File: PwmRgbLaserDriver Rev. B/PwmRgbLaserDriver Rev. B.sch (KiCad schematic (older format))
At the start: 40 parts

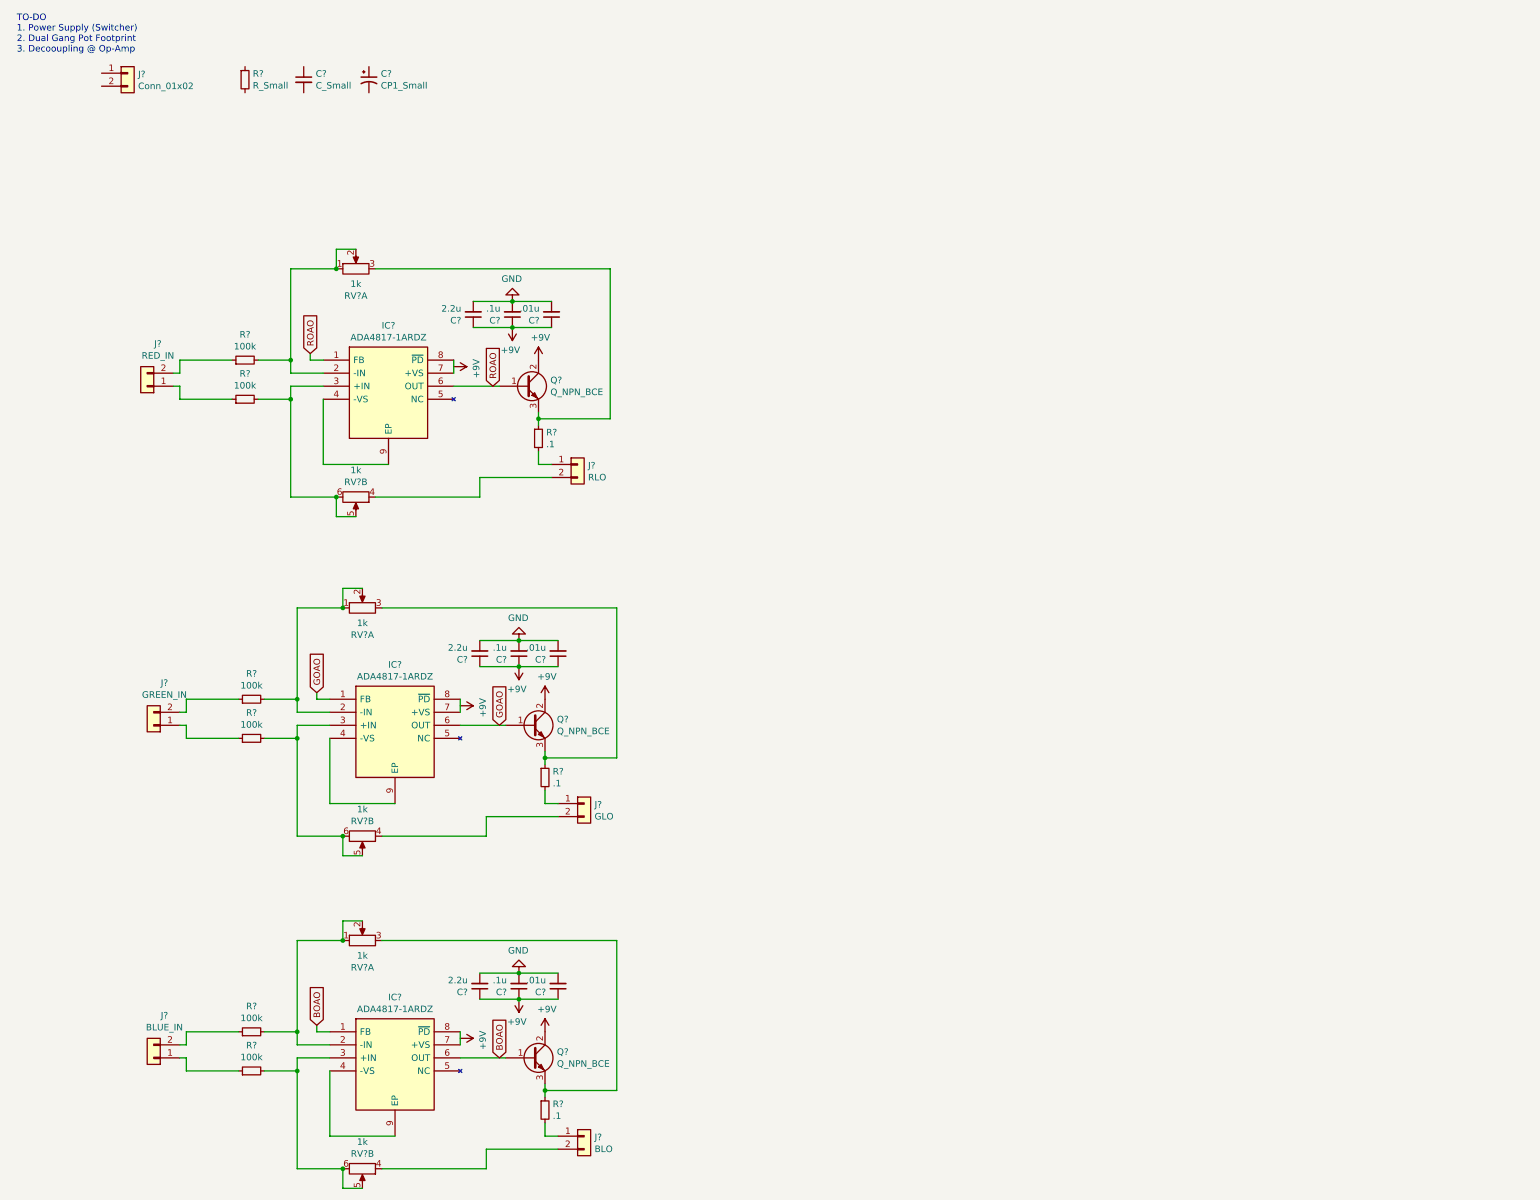
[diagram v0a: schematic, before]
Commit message: Switching Converter Added
This commit adds the switching converter for power.
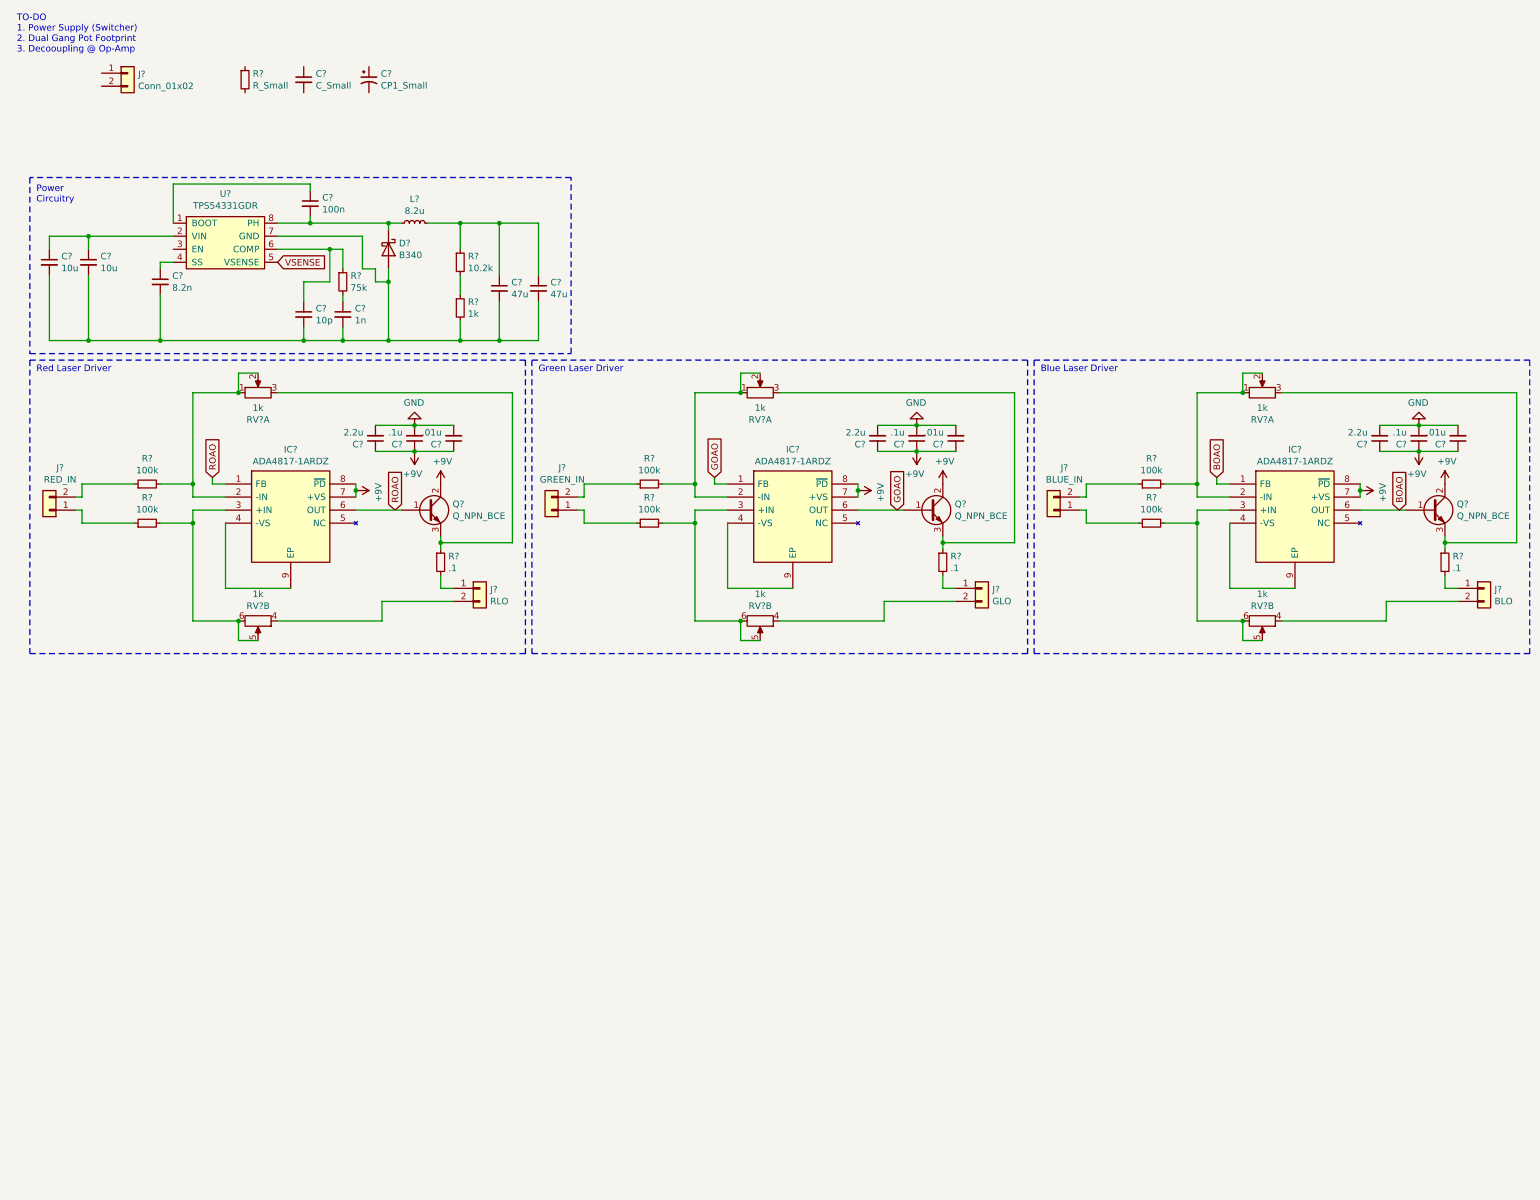
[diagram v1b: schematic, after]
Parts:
- added C?: 10p, symbol Device:C_Small
- added C?: 1n, symbol Device:C_Small
- added C?: 8.2n, symbol Device:C_Small
- added C? (x2): 47u, symbol Device:C_Small
- added C?: 100n, symbol Device:C_Small
- added C? (x2): 10u, symbol Device:C_Small
- added D?: B340, Diode_SMD:D_SMC, symbol Diode:B340
- added L?: 8.2u, symbol Device:L_Small
- added R?: 10.2k, symbol Device:R_Small
- added R?: 1k, symbol Device:R_Small
- added R?: 75k, symbol Device:R_Small
- added U?: TPS54331GDR, symbol SamacSys_Parts:TPS54331GDR
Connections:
- net +9V: now also IC?.7 (+VS), IC?.7 (+VS), IC?.7 (+VS), IC?.8 (~PD), IC?.8 (~PD), IC?.8 (~PD)
- new net: C?.1, U?.1 (BOOT)
- new net: C?.1, C?.1, U?.2 (VIN)
- new net: C?.1, U?.4 (SS)
- new net: C?.1, R?.1, U?.6 (COMP)
- new net: C?.2, C?.2, C?.2, C?.2, C?.2, C?.2, C?.2, D?.2 (A), R?.2, U?.7 (GND)
- new net: C?.2, D?.1 (K), L?.1, U?.8 (PH)
- new net: C?.1, R?.2
- new net: C?.1, C?.1, L?.2, R?.1
- new net: R?.1, R?.2
- new net VSENSE: U?.5 (VSENSE)
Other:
- note added: "Blue Laser Driver"
- note added: "Green Laser Driver"
- note added: "Power\nCircuitry"
- note added: "Red Laser Driver"
- moved on the sheet: C?, IC?, J?, Q?, R?, RV?A, RV?B

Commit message: Small Fixes
Added Enable pin resistor divider on switcher. Fixed grounding issues in drivers
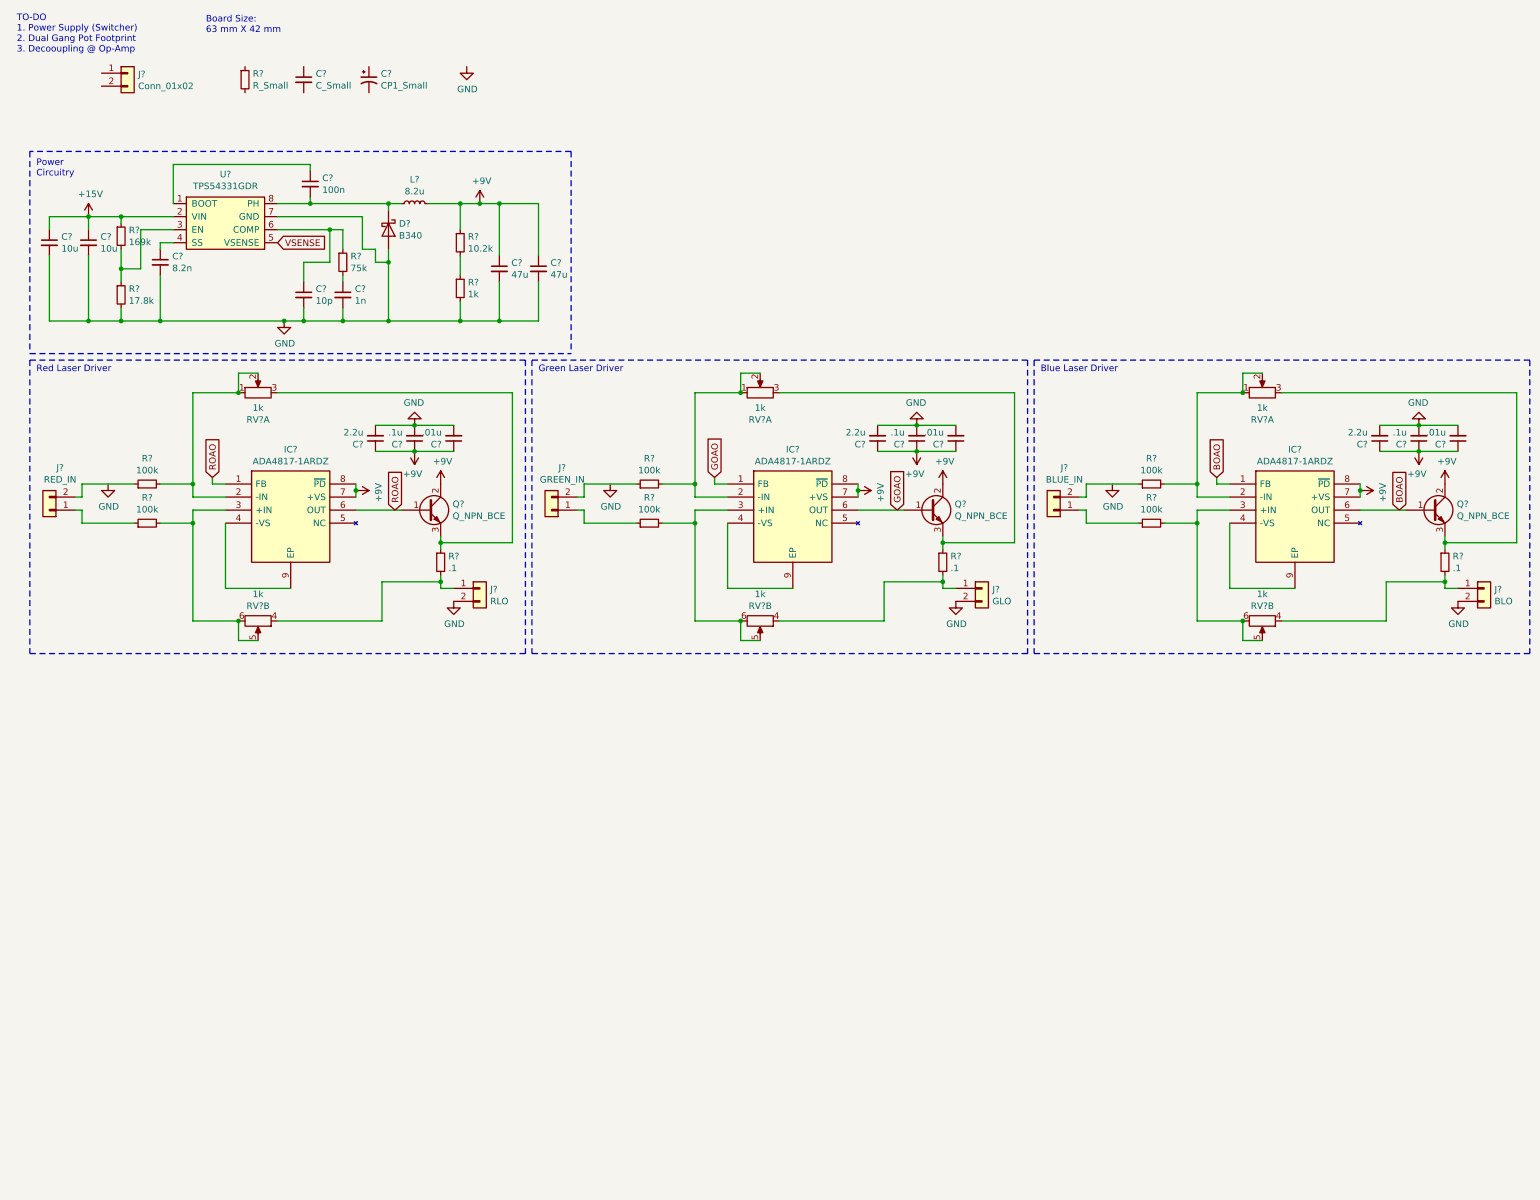
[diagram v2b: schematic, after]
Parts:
- added R?: 169k, symbol Device:R_Small
- added R?: 17.8k, symbol Device:R_Small
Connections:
- net +9V: now also C?.1, C?.1, L?.2, R?.1
- net GND: now also C?.2, C?.2, C?.2, C?.2, C?.2, C?.2, C?.2, D?.2 (A), J?.2 (Pin_2), J?.2 (Pin_2), J?.2 (Pin_2), R?.2, U?.7 (GND), R?.2
- net at RV?.4: now also J?.1 (Pin_1), R?.2; no longer J?.2 (Pin_2) (x3)
- net +15V: now reaches C?.1, C?.1, U?.2 (VIN)
- net +15V: now also R?.1
- net at U?.3 (EN): now also R?.1, R?.2
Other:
- note added: "Board Size:\n63 mm X 42 mm"
- moved on the sheet: C?, D?, L?, R?, U?

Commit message: TO-DO Update
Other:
- note added: "TO-DO\n1. Dual Gang Pot Footprint\n2. Shop for passives\n"
- note removed: "TO-DO\n1. Power Supply (Switcher)\n2. Dual Gang Pot Footprint\n3. Decooupling @ Op-Amp"
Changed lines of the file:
@@
 	1    0    0    -1
 $EndComp
-Text Notes 500  800  0    50   ~ 0
-TO-DO\n1. Power Supply (Switcher)\n2. Dual Gang Pot Footprint\n3. Decooupling @ Op-Amp
+Text Notes 500  750  0    50   ~ 0
+TO-DO\n1. Dual Gang Pot Footprint\n2. Shop for passives\n
 $Comp
 L Device:Q_NPN_BCE Q?

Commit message: Fixed Some Errors
Fixed some errors and updated the to-do list.
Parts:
- IC? (x3): symbol SamacSys_Parts:ADA4817-1ARDZ -> PwmRgbLaserDriver-Rev.-B-rescue:ADA4817-1ARDZ-SamacSys_Parts
- U?: symbol SamacSys_Parts:TPS54331GDR -> PwmRgbLaserDriver-Rev.-B-rescue:TPS54331GDR-SamacSys_Parts
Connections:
- net VSENSE: now also R?.1, R?.2
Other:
- note added: "TO-DO\n1. Dual Gang Pot Footprint\n2. Shop for passives\n3. Mounting Holes\n"
- note removed: "TO-DO\n1. Dual Gang Pot Footprint\n2. Shop for passives\n"
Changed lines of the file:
@@
 $EndDescr
 $Comp
-L SamacSys_Parts:ADA4817-1ARDZ IC?
+L PwmRgbLaserDriver-Rev.-B-rescue:ADA4817-1ARDZ-SamacSys_Parts IC?
 U 1 1 60DCA498
 P 2100 4100
@@
 	1    0    0    -1
 $EndComp
-Text Notes 500  750  0    50   ~ 0
-TO-DO\n1. Dual Gang Pot Footprint\n2. Shop for passives\n
+Text Notes 500  800  0    50   ~ 0
+TO-DO\n1. Dual Gang Pot Footprint\n2. Shop for passives\n3. Mounting Holes\n
 $Comp
 L Device:Q_NPN_BCE Q?
@@
 	2000 4100 2000 4050
 $Comp
-L SamacSys_Parts:ADA4817-1ARDZ IC?
+L PwmRgbLaserDriver-Rev.-B-rescue:ADA4817-1ARDZ-SamacSys_Parts IC?
 U 1 1 60E617A8
 P 5950 4100
@@
 	5850 4100 5850 4050
 $Comp
-L SamacSys_Parts:ADA4817-1ARDZ IC?
+L PwmRgbLaserDriver-Rev.-B-rescue:ADA4817-1ARDZ-SamacSys_Parts IC?
 U 1 1 60E84C66
 P 9800 4100
@@
 	9700 4100 9700 4050
 $Comp
-L SamacSys_Parts:TPS54331GDR U?
+L PwmRgbLaserDriver-Rev.-B-rescue:TPS54331GDR-SamacSys_Parts U?
 U 1 1 60EA0AF4
 P 2850 1700
@@
 Text Notes 1950 650  0    50   ~ 0
 Board Size:\n63 mm X 42 mm
+Text GLabel 3900 2400 0    50   Input ~ 0
+VSENSE
 $EndSCHEMATC
